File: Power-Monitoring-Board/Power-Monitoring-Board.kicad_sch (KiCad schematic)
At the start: 29 parts, among them J2 Conn_01x03_Pin, J3 Conn_01x03_Pin, U1 NUCLEO_L432KC, U2 ST7735R, U3 INA260AIPWR, U4 TPS562231DRLR

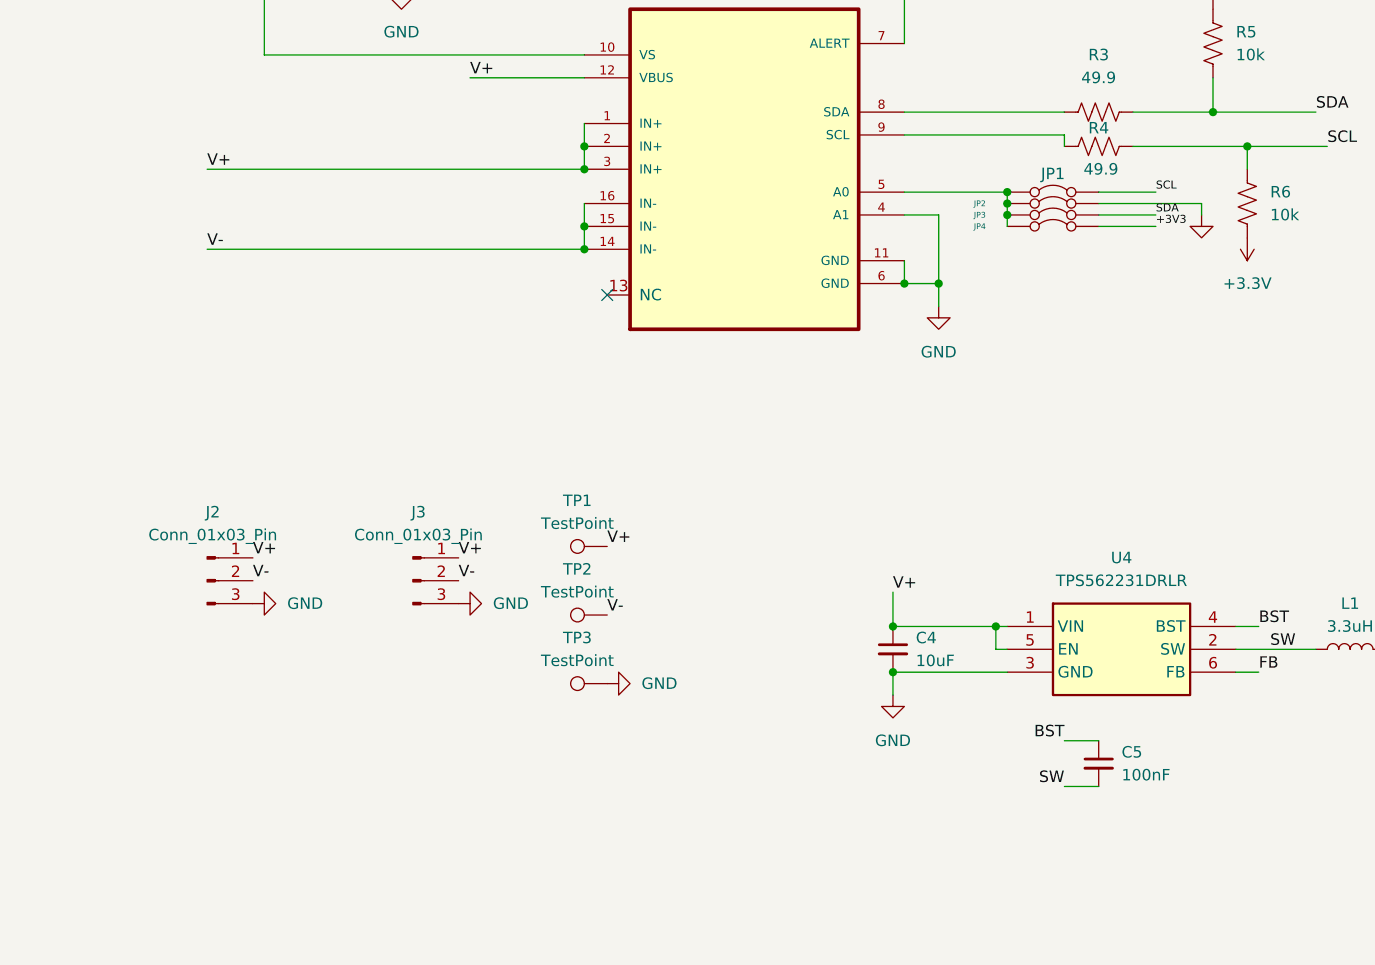
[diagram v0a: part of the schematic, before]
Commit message: update sch and footprints
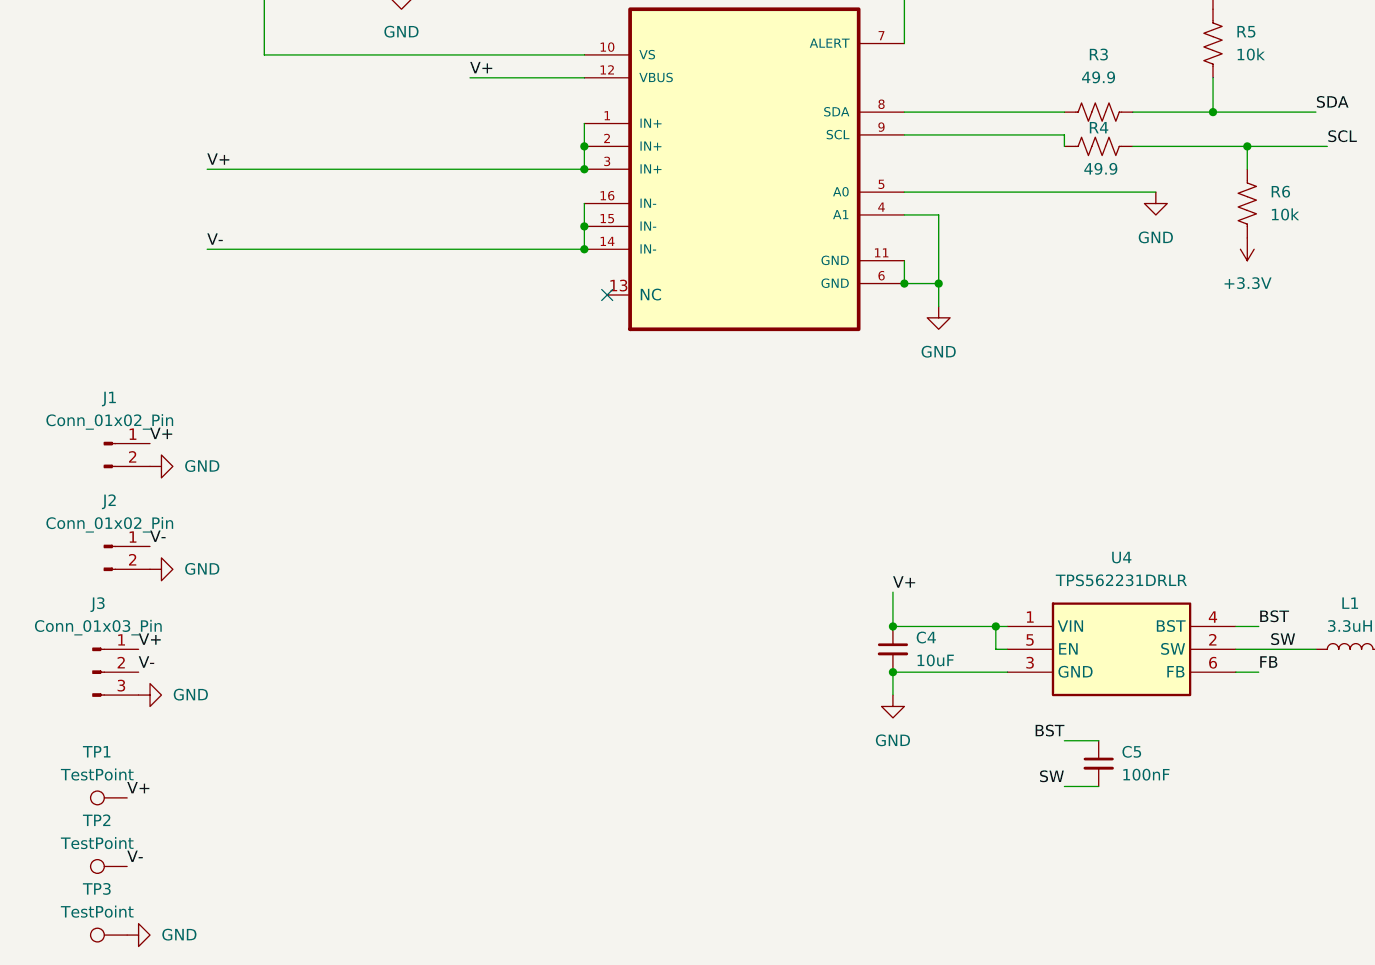
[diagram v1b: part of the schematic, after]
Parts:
- removed J2: Conn_01x03_Pin, symbol Connector:Conn_01x03_Pin
- removed JP1, JP2, JP3, JP4: Jumper_2_Bridged, Connector_PinHeader_2.54mm:PinHeader_1x02_P2.54mm_Horizontal, symbol Jumper:Jumper_2_Bridged
- added J1, J2: Conn_01x02_Pin, Connector_Molex:Molex_Micro-Fit_3.0_43045-0212_2x01_P3.00mm_Vertical, symbol Connector:Conn_01x02_Pin
- J3: footprint (none) -> Power-Monitoring:CONN_1988817
- TP1, TP2, TP3: footprint (none) -> TestPoint:TestPoint_Pad_D3.0mm
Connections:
- net GND: now also U3.5 (A0), J1.2 (Pin_2), J2.2 (Pin_2)
- net V+: now also J1.1 (Pin_1)
- net V-: now also J2.1 (Pin_1)
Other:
- moved on the sheet: J3, TP1, TP2, TP3

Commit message: the newst version of the board with all the stuff
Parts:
- removed C4: 10uF, Capacitor_SMD:C_0805_2012Metric, symbol Device:C_Small
- removed C5: 100nF, Capacitor_SMD:C_0805_2012Metric, symbol Device:C_Small
- removed J3: Conn_01x03_Pin, Power-Monitoring:CONN_1988817, symbol Connector:Conn_01x03_Pin
- removed L1: 3.3uH, Inductor_SMD:L_0805_2012Metric, symbol Device:L
- removed R7: 10k, Resistor_SMD:R_0805_2012Metric, symbol Device:R_US
- removed U4: TPS562231DRLR, Package_TO_SOT_SMD:SOT-563, symbol Power-Mon:TPS562231DRLR
- added C2, C4, C5: 1uF, Capacitor_SMD:C_0805_2012Metric, symbol Device:C
- added C3: 10nF, Capacitor_SMD:C_0805_2012Metric, symbol Device:C
- added D3: Batt_On_LED, LED_SMD:LED_0805_2012Metric, symbol Device:LED
- added IC1: XC6222D331MR-G, Power-Monitoring:SOT95P280X130-5N, symbol XC6222D331MR-G:XC6222D331MR-G
- added J3, J4, J5, J6: Conn_01x01_Pin, UTSVTConnectors:Banana_Jack_Horizontal, symbol Connector:Conn_01x01_Pin
- added J7, J8: Conn_01x02_Pin, Power-Monitoring:screw_termina2x1, symbol Connector:Conn_01x02_Pin
- added R11, R12, R3: 4.7k, Resistor_SMD:R_0805_2012Metric, symbol Device:R_US
- added R4: 1K, Resistor_SMD:R_0805_2012Metric, symbol Device:R_US
- added R5: 10k, Resistor_SMD:R_0805_2012Metric, symbol Device:R_US
- added SW1: GF-123-0054, Power-Monitoring:SW2_GF-123-0054_CWI, symbol 2025-01-08_04-45-24:GF-123-0054
- added TP4, TP5, TP6: TestPoint, TestPoint:TestPoint_Plated_Hole_D2.0mm, symbol Connector:TestPoint
- added U2: CR2450, Battery:BatteryHolder_Keystone_103_1x20mm, symbol cr2450-Lir2450:CR2450
- added U3: MAX17043G+U, Power-Monitoring:21-0174B_MXM, symbol 2025-01-08_04-59-47:MAX17043G+U
- J1, J2: footprint Connector_Molex:Molex_Micro-Fit_3.0_43045-0212_2x01_P3.00mm_Vertical -> UTSVTConnectors:Molex_MicroFit3.0_1x2xP3.00mm_PolarizingPeg_Vertical
- R8: value 10k -> 150
- TP1, TP2, TP3: footprint TestPoint:TestPoint_Pad_D3.0mm -> TestPoint:TestPoint_Plated_Hole_D2.0mm
- renumbered C2 to C6, C3 to C7, R2 to R1, R6 to R10, R1 to R2, R3 to R6, R4 to R7, R5 to R9, U3 to U1, U1 to U4, U2 to U5
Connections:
- net +3.3V: now also C5.2, IC1.5 (VOUT), R11.1, R12.1, TP5.1; no longer U5.10 (LITE)
- net CARD_CS: now also U4.CN4_12 (PA0); no longer U4.CN4_6 (PA7)
- net DC: now also U4.CN4_11 (PA1); no longer U4.CN3_5 (PA12)
- net GND: now also U5.10 (LITE), C2.1, C3.1, C4.1, C5.1, D3.1 (K), IC1.2 (VSS), J5.1 (Pin_1), J6.1 (Pin_1), J7.2 (Pin_2), J8.2 (Pin_2), TP4.1, U2.2 (-), U3.1 (CTG), U3.4 (GND), U3.6 (QSTRT), U3.9 (EPAD); no longer R8.2
- net MOSI: now also U4.CN4_6 (PA7); no longer U4.CN3_14 (PB5)
- net RESET: now also U4.CN4_10 (PA3); no longer U4.CN3_12 (PA8)
- net SCK: now also U4.CN4_8 (PA5); no longer U4.CN4_15 (PB3)
- net SCL: now also U4.CN3_8 (PB6); no longer U4.CN3_1 (PA9)
- net SDA: now also U4.CN3_7 (PB7); no longer U4.CN3_2 (PA10)
- net TFT_CS: now also U4.CN4_15 (PB3); no longer U4.CN3_13 (PA11)
- net V+: now also J3.1 (Pin_1), J7.1 (Pin_1)
- net V-: now also J4.1 (Pin_1), J8.1 (Pin_1)
- net FB: no longer names the net of R8.1
- net FB: now also C4.2, IC1.1 (VIN), IC1.3 (CE), R3.1, R4.1, R5.2, SW1.2, TP6.1
- new net: C2.2, R4.2, U3.2 (CELL)
- new net: C3.2, R8.2, U3.3 (VDD)
- new net: D3.2 (A), R5.1
- new net: SW1.1, U2.1 (+)
- new net ALERT: R3.2, U3.5 (*ALRT), U4.CN3_14 (PB5)
- new net SCL_M: R12.2, U3.7 (SCL), U4.CN3_1 (PA9)
- new net SDA_M: R11.2, U3.8 (SDA), U4.CN3_2 (PA10)
- no-connect marks 21 -> 18
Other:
- moved on the sheet: D1, D2, R1, R2, U4

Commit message: changes
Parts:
- removed R6, R7: 49.9, Resistor_SMD:R_0805_2012Metric, symbol Device:R_US
- added C8: 0.1uF, Capacitor_SMD:C_0805_2012Metric, symbol Device:C
- added R13: 10k, Resistor_SMD:R_0805_2012Metric, symbol Device:R_US
- C1: value 1uF -> 0.1uF
- C5: value 1uF -> 2.2uF
- R11, R12: value 4.7k -> 10k
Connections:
- net ALERT: now also U4.CN3_1 (PA9); no longer U4.CN3_14 (PB5)
- net GND: now also C8.1, R13.1
- net SCL: now also R12.2, U1.9 (SCL), U3.7 (SCL)
- net SDA: now also R11.2, U1.8 (SDA), U3.8 (SDA)
- net V+: now also C8.2
- net Batt: now reaches C4.2, IC1.1 (VIN), IC1.3 (CE), R3.1, R4.1, R5.2, R8.1, SW1.2, TP6.1
- net Batt: now also R13.2
- net MISO: now reaches U5.9 (MISO)
- net MISO: now also U4.CN4_5 (PA2)
- removed net SCL_M: R12.2, U3.7 (SCL), U4.CN3_1 (PA9)
- removed net SDA_M: R11.2, U3.8 (SDA), U4.CN3_2 (PA10)
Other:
- note added: "Battery + LDO + SOC Tracker"
- note added: "Inputs"
- note added: "LCD"
- note added: "Nucleo"
- note added: "Power Monitoring Chp"
- note added: "Test Points"
- moved on the sheet: C1, C2, C3, C4, C5, C6, C7, D1, D2, D3, IC1, J1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
